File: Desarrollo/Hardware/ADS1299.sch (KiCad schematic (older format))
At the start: 31 parts, among them J2 I/O's Multi Propósito, U10 ADS1299, U14 OPA2376_NI

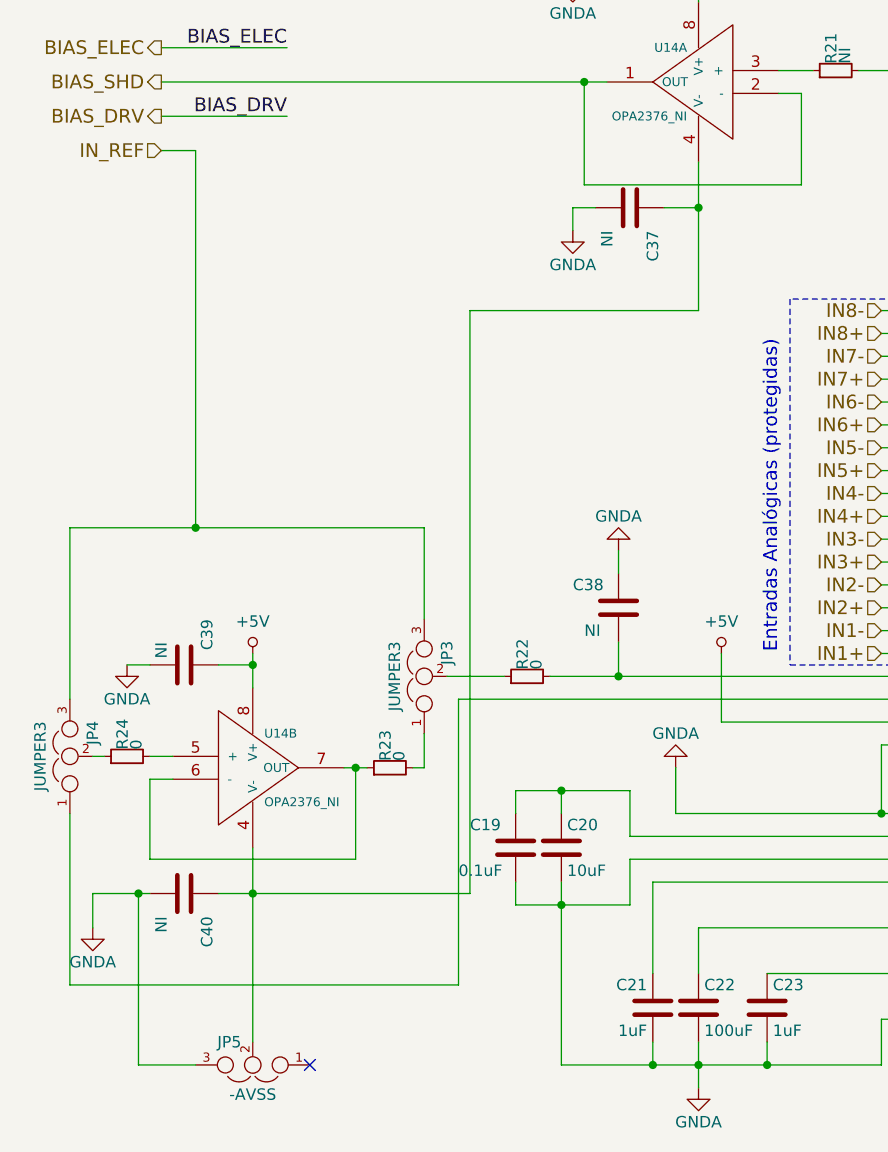
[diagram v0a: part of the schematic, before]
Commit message: Revert "Finalización de primer ruteo estimado. Revisión de cantidad de v"
This reverts commit b379d941abb4cafe5355ba8bbe61a2a3831aeef6.
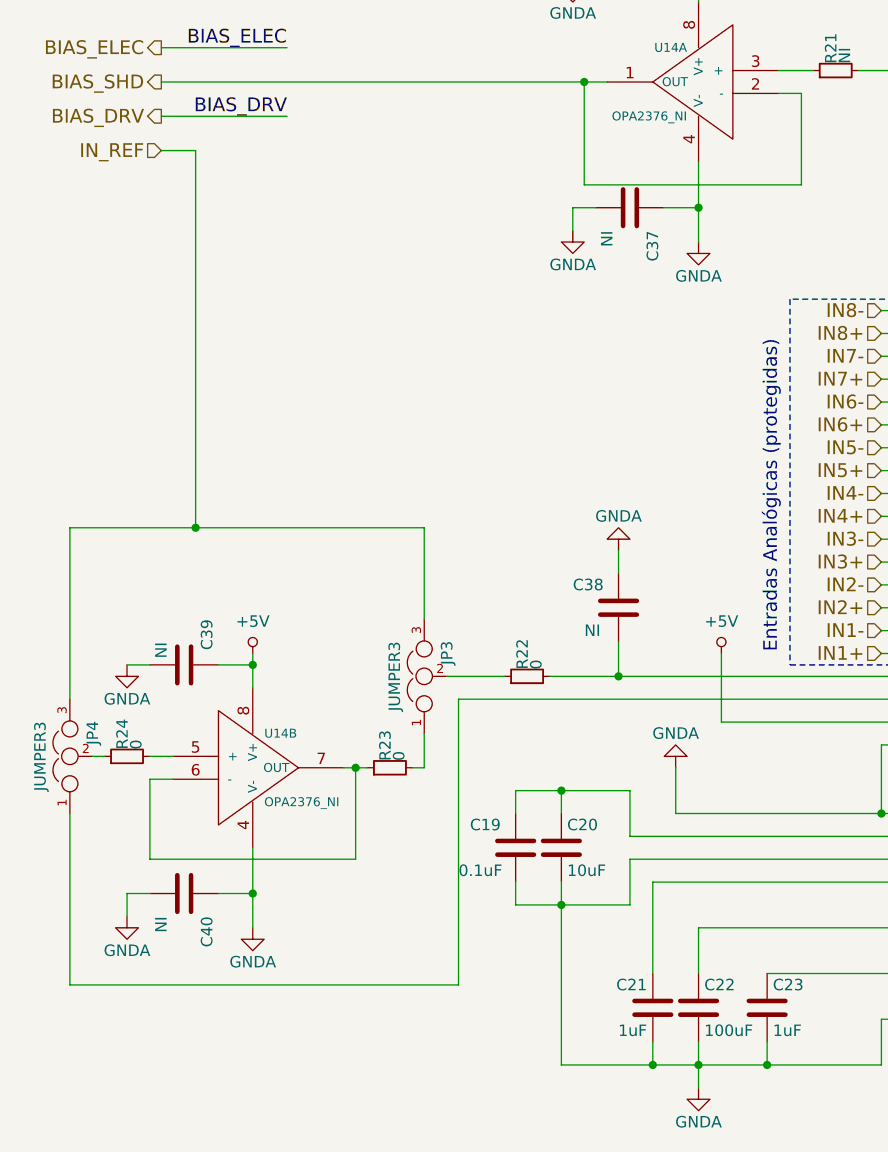
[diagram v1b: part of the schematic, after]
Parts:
- removed JP5: -AVSS, Pin_Headers:Pin_Header_Straight_1x03, symbol JUMPER3
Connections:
- net GNDA: now also C37.1, C40.1, U14.4 (V-), U14.4 (V-)
- no-connect marks 5 -> 4
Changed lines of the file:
@@
 encoding utf-8
 Sheet 3 4
-Title "ADS1299"
+Title ""
 Date ""
-Rev "1.0"
-Comp "Bruno Javier Cesario"
+Rev ""
+Comp ""
 Comment1 ""
 Comment2 ""
@@
 P 7050 3800
 AR Path="/57CB1828" Ref="#PWR?"  Part="1"
-AR Path="/57BDC369/57CB1828" Ref="#PWR010"  Part="1"
-F 0 "#PWR010" H 7050 3650 50  0001 C CNN
+AR Path="/57BDC369/57CB1828" Ref="#PWR09"  Part="1"
+F 0 "#PWR09" H 7050 3650 50  0001 C CNN
 F 1 "+3.3V" H 7050 3940 50  0000 C CNN
 F 2 "" H 7050 3800 50  0000 C CNN
@@
 P 9000 2400
 AR Path="/57CB18B2" Ref="#PWR?"  Part="1"
-AR Path="/57BDC369/57CB18B2" Ref="#PWR011"  Part="1"
-F 0 "#PWR011" H 9000 2250 50  0001 C CNN
+AR Path="/57BDC369/57CB18B2" Ref="#PWR010"  Part="1"
+F 0 "#PWR010" H 9000 2250 50  0001 C CNN
 F 1 "+3.3V" H 9000 2540 50  0000 C CNN
 F 2 "" H 9000 2400 50  0000 C CNN
@@
 $EndComp
 $Comp
-L +5V #PWR012
+L +5V #PWR011
 U 1 1 57CB18ED
 P 9900 2400
-F 0 "#PWR012" H 9900 2250 50  0001 C CNN
+F 0 "#PWR011" H 9900 2250 50  0001 C CNN
 F 1 "+5V" H 9900 2540 50  0000 C CNN
 F 2 "" H 9900 2400 50  0000 C CNN
@@
 $EndComp
 $Comp
-L Earth #PWR013
+L Earth #PWR012
 U 1 1 57CB195C
 P 4500 5600
-F 0 "#PWR013" H 4500 5350 50  0001 C CNN
+F 0 "#PWR012" H 4500 5350 50  0001 C CNN
 F 1 "Earth" H 4500 5450 50  0001 C CNN
 F 2 "" H 4500 5600 50  0000 C CNN
@@
 $EndComp
 $Comp
-L Earth #PWR014
+L Earth #PWR013
 U 1 1 57CB198A
 P 6500 5500
-F 0 "#PWR014" H 6500 5250 50  0001 C CNN
+F 0 "#PWR013" H 6500 5250 50  0001 C CNN
 F 1 "Earth" H 6500 5350 50  0001 C CNN
 F 2 "" H 6500 5500 50  0000 C CNN
@@
 $EndComp
 $Comp
-L Earth #PWR015
+L Earth #PWR014
 U 1 1 57CB19B8
 P 7200 4500
-F 0 "#PWR015" H 7200 4250 50  0001 C CNN
+F 0 "#PWR014" H 7200 4250 50  0001 C CNN
 F 1 "Earth" H 7200 4350 50  0001 C CNN
 F 2 "" H 7200 4500 50  0000 C CNN
@@
 $EndComp
 $Comp
-L Earth #PWR016
+L Earth #PWR015
 U 1 1 57CB19E6
 P 6650 3500
-F 0 "#PWR016" H 6650 3250 50  0001 C CNN
+F 0 "#PWR015" H 6650 3250 50  0001 C CNN
 F 1 "Earth" H 6650 3350 50  0001 C CNN
 F 2 "" H 6650 3500 50  0000 C CNN
@@
 $EndComp
 $Comp
-L Earth #PWR017
+L Earth #PWR016
 U 1 1 57CB1A14
 P 9000 3100
-F 0 "#PWR017" H 9000 2850 50  0001 C CNN
+F 0 "#PWR016" H 9000 2850 50  0001 C CNN
 F 1 "Earth" H 9000 2950 50  0001 C CNN
 F 2 "" H 9000 3100 50  0000 C CNN
@@
 $EndComp
 $Comp
-L GNDA-RESCUE-PonchoERG #PWR018
+L GNDA-RESCUE-PonchoERG #PWR017
 U 1 1 57CB1A83
 P 7400 2700
-F 0 "#PWR018" H 7400 2450 50  0001 C CNN
+F 0 "#PWR017" H 7400 2450 50  0001 C CNN
 F 1 "GNDA" H 7400 2550 50  0000 C CNN
 F 2 "" H 7400 2700 50  0000 C CNN
@@
 $EndComp
 $Comp
-L GNDA-RESCUE-PonchoERG #PWR019
+L GNDA-RESCUE-PonchoERG #PWR018
 U 1 1 57CB1AB1
 P 9900 3100
-F 0 "#PWR019" H 9900 2850 50  0001 C CNN
+F 0 "#PWR018" H 9900 2850 50  0001 C CNN
 F 1 "GNDA" H 9900 2950 50  0000 C CNN
 F 2 "" H 9900 3100 50  0000 C CNN
@@
 $EndComp
 $Comp
-L GNDA-RESCUE-PonchoERG #PWR020
+L GNDA-RESCUE-PonchoERG #PWR019
 U 1 1 57CB1ADF
 P 3500 4200
-F 0 "#PWR020" H 3500 3950 50  0001 C CNN
+F 0 "#PWR019" H 3500 3950 50  0001 C CNN
 F 1 "GNDA" H 3500 4050 50  0000 C CNN
 F 2 "" H 3500 4200 50  0000 C CNN
@@
 $EndComp
 $Comp
-L GNDA-RESCUE-PonchoERG #PWR021
+L GNDA-RESCUE-PonchoERG #PWR020
 U 1 1 57CB1B0D
 P 3600 5600
-F 0 "#PWR021" H 3600 5350 50  0001 C CNN
+F 0 "#PWR020" H 3600 5350 50  0001 C CNN
 F 1 "GNDA" H 3600 5450 50  0000 C CNN
 F 2 "" H 3600 5600 50  0000 C CNN
@@
 $EndComp
 $Comp
-L GNDA-RESCUE-PonchoERG #PWR022
+L GNDA-RESCUE-PonchoERG #PWR021
 U 1 1 57CB1B3B
 P 7750 3700
-F 0 "#PWR022" H 7750 3450 50  0001 C CNN
+F 0 "#PWR021" H 7750 3450 50  0001 C CNN
 F 1 "GNDA" H 7750 3550 50  0000 C CNN
 F 2 "" H 7750 3700 50  0000 C CNN
@@
 $EndComp
 $Comp
-L +5V #PWR023
+L +5V #PWR022
 U 1 1 57CB3AA5
 P 7100 2600
-F 0 "#PWR023" H 7100 2450 50  0001 C CNN
+F 0 "#PWR022" H 7100 2450 50  0001 C CNN
 F 1 "+5V" H 7100 2740 50  0000 C CNN
 F 2 "" H 7100 2600 50  0000 C CNN
@@
 $EndComp
 $Comp
-L +5V #PWR024
+L +5V #PWR023
 U 1 1 57CB3AD3
 P 3700 3700
-F 0 "#PWR024" H 3700 3550 50  0001 C CNN
+F 0 "#PWR023" H 3700 3550 50  0001 C CNN
 F 1 "+5V" H 3700 3840 50  0000 C CNN
 F 2 "" H 3700 3700 50  0000 C CNN
@@
 	4550 1550 6250 1550
 Connection ~ 3600 750
+$Comp
+L GNDA-RESCUE-PonchoERG #PWR024
+U 1 1 57CCF983
+P 3600 1900
+F 0 "#PWR024" H 3600 1650 50  0001 C CNN
+F 1 "GNDA" H 3600 1750 50  0000 C CNN
+F 2 "" H 3600 1900 50  0000 C CNN
+F 3 "" H 3600 1900 50  0000 C CNN
+	1    3600 1900
+	1    0    0    -1
+$EndComp
 Connection ~ 3600 1750
 $Comp
@@
 	1    0    0    -1
 $EndComp
+Wire Wire Line
+	3600 1550 3600 1900
 $Comp
 L GNDA-RESCUE-PonchoERG #PWR028
@@
 $EndComp
 Wire Wire Line
-	1500 4750 2600 4750
+	1500 4750 1650 4750
+$Comp
+L GNDA-RESCUE-PonchoERG #PWR031
+U 1 1 57CDA7F0
+P 1650 4900
+F 0 "#PWR031" H 1650 4650 50  0001 C CNN
+F 1 "GNDA" H 1650 4750 50  0000 C CNN
+F 2 "" H 1650 4900 50  0000 C CNN
+F 3 "" H 1650 4900 50  0000 C CNN
+	1    1650 4900
+	1    0    0    -1
+$EndComp
 Connection ~ 1650 4750
 $Comp
-L GNDA-RESCUE-PonchoERG #PWR031
+L GNDA-RESCUE-PonchoERG #PWR032
 U 1 1 57CDA7F7
-P 950 4900
-F 0 "#PWR031" H 950 4650 50  0001 C CNN
-F 1 "GNDA" H 950 4750 50  0000 C CNN
-F 2 "" H 950 4900 50  0000 C CNN
-F 3 "" H 950 4900 50  0000 C CNN
-	1    950  4900
-	1    0    0    -1
-$EndComp
-Wire Wire Line
-	1650 4550 1650 5400
+P 1100 4850
+F 0 "#PWR032" H 1100 4600 50  0001 C CNN
+F 1 "GNDA" H 1100 4700 50  0000 C CNN
+F 2 "" H 1100 4850 50  0000 C CNN
+F 3 "" H 1100 4850 50  0000 C CNN
+	1    1100 4850
+	1    0    0    -1
+$EndComp
+Wire Wire Line
+	1100 4850 1100 4750
+Wire Wire Line
+	1100 4750 1200 4750
+Wire Wire Line
+	1650 4550 1650 4900
 Wire Wire Line
 	1250 1500 1400 1500
@@
 Text Notes 9700 900  0    60   ~ 0
 Nota:\n\nNI: Not Installed
-Wire Wire Line
-	2600 4750 2600 2200
-Wire Wire Line
-	2600 2200 3600 2200
-Wire Wire Line
-	3600 2200 3600 1550
-Wire Wire Line
-	950  4900 950  4750
-Wire Wire Line
-	950  4750 1200 4750
-$Comp
-L JUMPER3 JP5
-U 1 1 57CFEB0F
-P 1650 5500
-F 0 "JP5" H 1700 5400 50  0000 L CNN
-F 1 "-AVSS" H 1650 5600 50  0000 C BNN
-F 2 "Pin_Headers:Pin_Header_Straight_1x03" H 1650 5500 50  0001 C CNN
-F 3 "" H 1650 5500 50  0000 C CNN
-	1    1650 5500
-	-1   0    0    1
-$EndComp
-Wire Wire Line
-	1400 5500 1150 5500
-Wire Wire Line
-	1150 5500 1150 4750
-Connection ~ 1150 4750
-NoConn ~ 1900 5500
 $EndSCHEMATC
